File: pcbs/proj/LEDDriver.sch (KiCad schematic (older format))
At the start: 12 parts, among them J1 Conn_02x32_Counter_Clockwise, J2 Conn_02x03_Odd_Even, J3 Conn_01x05, U1 DAC101C085

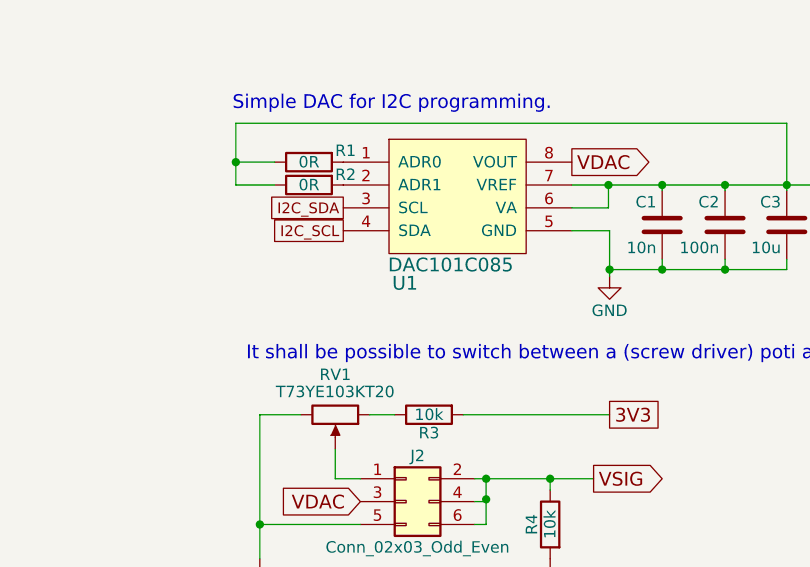
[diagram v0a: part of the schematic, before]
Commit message: All components placed.
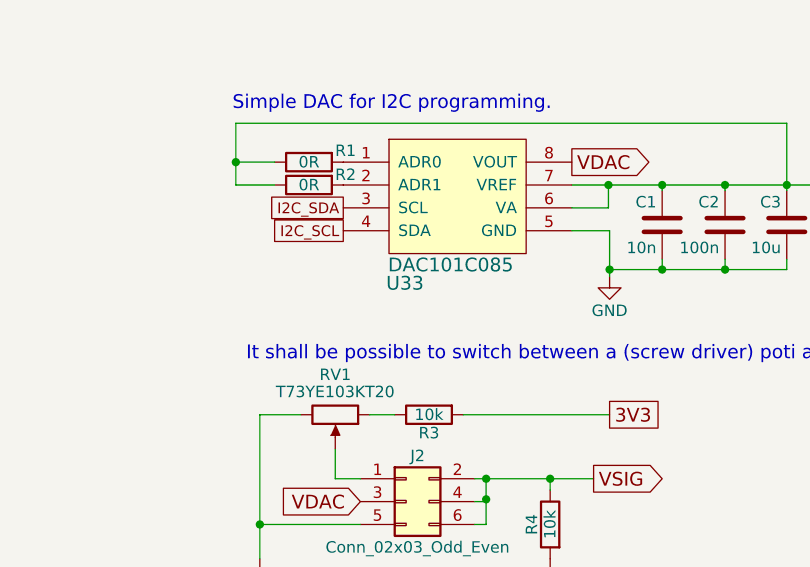
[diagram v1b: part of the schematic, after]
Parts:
- renumbered U1 to U33
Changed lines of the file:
@@
 $EndComp
 $Comp
-L DAC101C085 U1
+L DAC101C085 U33
 U 1 1 5A10AF74
 P 8435 2445
-F 0 "U1" H 8205 2015 60  0000 C CNN
+F 0 "U33" H 8205 2015 60  0000 C CNN
 F 1 "DAC101C085" H 8405 2095 60  0000 C CNN
 F 2 "SSOP:VSSOP-8_3.0x3.0mm_Pitch0.65mm" H 8335 2345 60  0001 C CNN

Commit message: Started eliminating DRC errors.
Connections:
- net GND: no longer J2.5 (Pin_5)
- net I2C_SCL: now also U33.3 (SCL); no longer U33.4 (SDA)
- net I2C_SDA: now also U33.4 (SDA); no longer U33.3 (SCL)
- net LIGHT_INT: now reaches J3.5 (Pin_5)
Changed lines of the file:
@@
 	-1   0    0    -1
 $EndComp
+Text GLabel 7935 2645 0    47   UnSpc ~ 0
+I2C_SDA
 Text GLabel 7935 2545 0    47   UnSpc ~ 0
-I2C_SDA
-Text GLabel 7935 2645 0    47   UnSpc ~ 0
 I2C_SCL
 $Comp
@@
 Text Notes 1700 900  0    60   ~ 0
 32 x 2 = 64 stages. 1 stage consists out of 4 LEDs.
-NoConn ~ 8150 5100
 Wire Wire Line
 	2530 1170 2565 1170
@@
 Connection ~ 8560 3820
 Wire Wire Line
-	8010 3930 7570 3930
-Wire Wire Line
 	7570 3450 7570 4080
 Wire Wire Line
 	7570 3450 7750 3450
-Connection ~ 7570 3930
 Wire Wire Line
 	8840 3780 8840 3730
@@
 Text GLabel 10015 2445 2    60   UnSpc ~ 0
 3V3
+Text GLabel 8150 5100 0    47   UnSpc ~ 0
+LIGHT_INT
+NoConn ~ 8010 3930
 $EndSCHEMATC
